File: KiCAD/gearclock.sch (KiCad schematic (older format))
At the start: 39 parts, among them IC1 ATMEGA328P, P10 CD2, P13 CD1, P14 I/O, P15 I/O, P16 I/O, P2 BAT, P4 MOTOR_L, P5 MOTOR_R, P6 LiPo, P7 GPS, P8 FTDI, P9 ISP, SW1 RST, U1 3V3, X1 8MHz

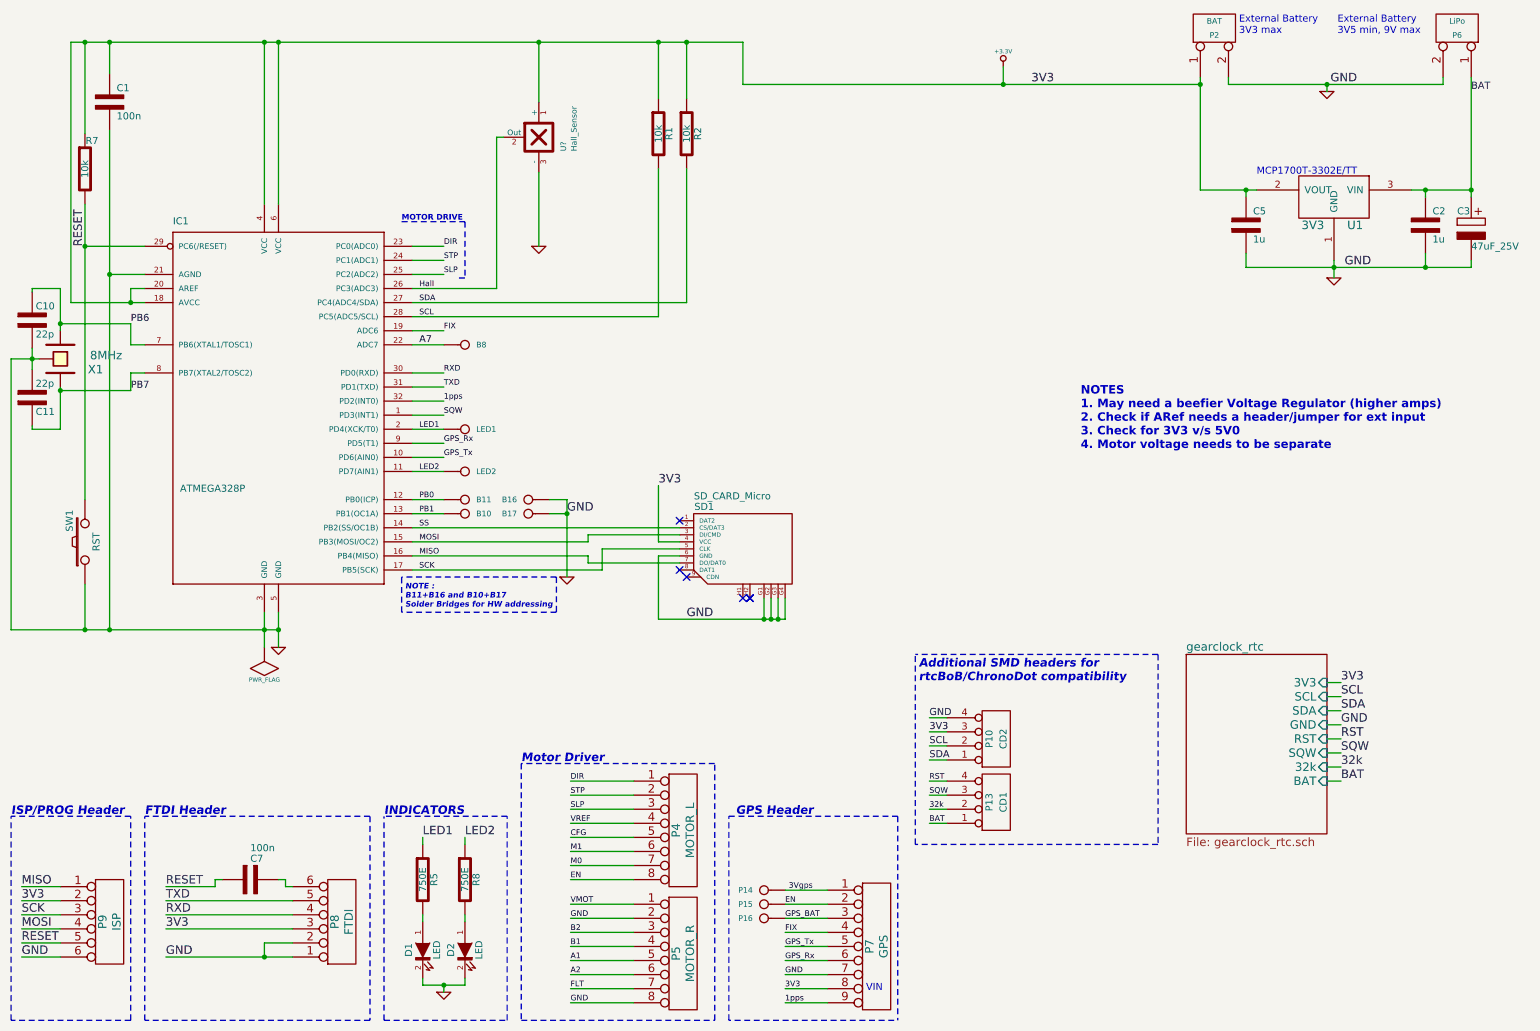
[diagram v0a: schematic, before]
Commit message: GearClock schematic needs review
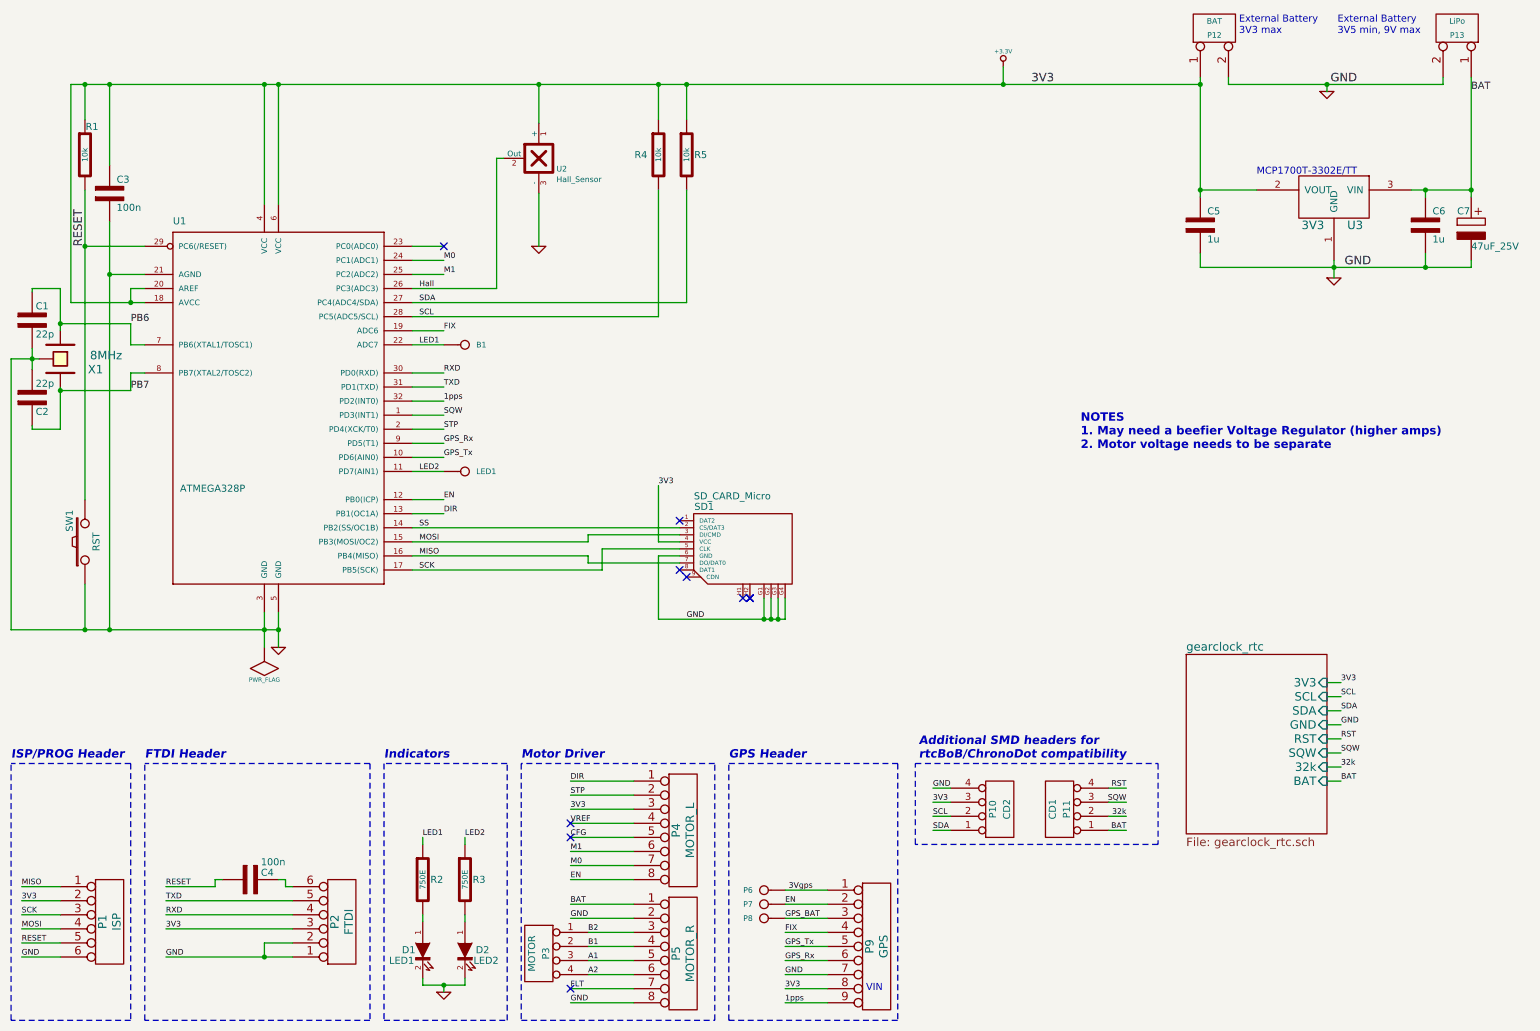
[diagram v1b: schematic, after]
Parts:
- removed B10, B11, B16, B17: I/O, ArthurC Lib:I%2fO_ADR, symbol I/O
- removed LED1: I/O, ArthurC Lib:I%2fO, symbol I/O
- added P3: MOTOR, symbol CONN_4
- D1: value LED -> LED1
- D2: value LED -> LED2
- gave numbers to parts that had none: 1
- renumbered B8 to B1, C10 to C1, C11 to C2, C1 to C3, C7 to C4, C2 to C6, C3 to C7, LED2 to LED1, P9 to P1, P13 to P11, P2 to P12, P6 to P13, P8 to P2, P14 to P6, P15 to P7, P16 to P8, P7 to P9, R7 to R1, R5 to R2, R8 to R3, R1 to R4, R2 to R5, IC1 to U1, U1 to U3
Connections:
- net A7 is gone; now on net LED1: B1.1, U1.22 (ADC7)
- net PB0 is gone; now on net EN: U1.12 (PB0(ICP))
- net PB1 is gone; now on net DIR: U1.13 (PB1(OC1A))
- net VMOT is gone; now on net BAT: P5.1
- net +3.3V: now also P4.3
- net A1: now also P3.3 (P3)
- net A2: now also P3.4 (P4)
- net B1: now also P3.2 (P2)
- net B2: now also P3.1 (P1)
- net DIR: no longer U1.23 (PC0(ADC0))
- net LED1: no longer U1.2 (PD4(XCK/T0))
- net M0: now also U1.24 (PC1(ADC1))
- net M1: now also U1.25 (PC2(ADC2))
- net STP: now also U1.2 (PD4(XCK/T0)); no longer U1.24 (PC1(ADC1))
- removed net SLP: P4.3, U1.25 (PC2(ADC2))
- no-connect marks 6 -> 10
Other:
- note added: "Indicators"
- note added: "NOTES\n1. May need a beefier Voltage Regulator (higher amps)\n2. Motor voltage needs to be separate"
- note removed: "INDICATORS"
- note removed: "MOTOR DRIVE"
- note removed: "NOTE :\nB11+B16 and B10+B17\nSolder Bridges for HW addressing"
- note removed: "NOTES\n1. May need a beefier Voltage Regulator (higher amps)\n2. Check if ARef needs a header/jumper for ext input\n3. Check for 3V3 v/s 5V0\n4. Motor voltage needs to be separate"
- moved on the sheet: C3, C5, P10, P11, R1, R4, R5, U2

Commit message: GearClock schematic mods
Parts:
- P4: value MOTOR_L -> MOTOR_R
- P5: value MOTOR_R -> MOTOR_L
- renumbered B1 to A8, LED1 to D7
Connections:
- net +3.3V: now also P4.6; no longer P4.3
- net CFG: now also P4.4; no longer P4.5
- net DIR: now also P4.8; no longer P4.1
- net EN: now also P4.1; no longer P4.8, P7.1, P9.2
- net Hall: now also U1.22 (ADC7); no longer U1.26 (PC3(ADC3))
- net LED1: now also U1.26 (PC3(ADC3)); no longer U1.22 (ADC7)
- net M0: now also P4.2; no longer P4.7
- net M1: now also P4.3; no longer P4.6
- net STP: now also P4.7; no longer P4.2
- net VREF: now also P4.5; no longer P4.4
- net GPS_EN: now reaches U1.23 (PC0(ADC0))
- net GPS_EN: now also P7.1, P9.2
- no-connect marks 10 -> 9
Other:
- moved on the sheet: A8
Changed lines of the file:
@@
 	3400 2250 3625 2250
 Wire Wire Line
-	3400 2950 3625 2950
+	4000 2950 3400 2950
 Wire Wire Line
 	3400 4150 3625 4150
@@
 	550  4975 2450 4975
 Wire Wire Line
-	4000 1625 4000 2550
-Wire Wire Line
-	4000 2550 3400 2550
+	4000 1625 4000 2950
 Wire Wire Line
 	4300 2250 4300 1875
@@
 P 5325 6400
 F 0 "P4" V 5275 6400 60  0000 C CNN
-F 1 "MOTOR_L" V 5375 6400 60  0000 C CNN
+F 1 "MOTOR_R" V 5375 6400 60  0000 C CNN
 F 2 "ArthurC Lib:PIN_ARRAY-6X1" H 5325 6400 60  0001 C CNN
 F 3 "" H 5325 6400 60  0001 C CNN
 	1    5325 6400
-	1    0    0    -1
+	1    0    0    1
 $EndComp
 Text Label 10000 5650 0    40   ~ 0
@@
 $EndComp
 $Comp
-L I/O B1
+L I/O A8
 U 1 1 4DCD1D4C
-P 3775 2950
-F 0 "B1" H 3855 2950 40  0000 L CNN
-F 1 "I/O" H 3775 3005 30  0001 C CNN
-F 2 "ArthurC Lib:I%2fO" H 3775 2950 60  0001 C CNN
-F 3 "" H 3775 2950 60  0001 C CNN
-	1    3775 2950
+P 3775 2550
+F 0 "A8" H 3855 2550 40  0000 L CNN
+F 1 "I/O" H 3775 2605 30  0001 C CNN
+F 2 "ArthurC Lib:I%2fO" H 3775 2550 60  0001 C CNN
+F 3 "" H 3775 2550 60  0001 C CNN
+	1    3775 2550
 	1    0    0    -1
 $EndComp
@@
 Text Label 3625 2450 0    40   ~ 0
 M1
-Text Label 3450 2550 0    40   ~ 0
+Text Label 3450 2950 0    40   ~ 0
 Hall
 Text Label 3625 3150 0    40   ~ 0
@@
 GPS_BAT
 Text Label 6050 6925 0    40   ~ 0
-EN
+GPS_EN
 Text Label 6050 7125 0    40   ~ 0
 FIX
@@
 Connection ~ 10600 2400
 $Comp
-L I/O LED1
-U 1 1 53809775
-P 3775 3850
-F 0 "LED1" H 3855 3850 40  0000 L CNN
-F 1 "I/O" H 3775 3905 30  0001 C CNN
-F 2 "ArthurC Lib:I%2fO" H 3775 3850 60  0001 C CNN
-F 3 "" H 3775 3850 60  0001 C CNN
-	1    3775 3850
-	1    0    0    -1
-$EndComp
-$Comp
 L CONN_8 P5
 U 1 1 4E241CD6
 P 5325 7275
 F 0 "P5" V 5275 7275 60  0000 C CNN
-F 1 "MOTOR_R" V 5375 7275 60  0000 C CNN
+F 1 "MOTOR_L" V 5375 7275 60  0000 C CNN
 F 2 "ArthurC Lib:PIN_ARRAY-6X1" H 5325 7275 60  0001 C CNN
 F 3 "" H 5325 7275 60  0001 C CNN
@@
 Text Label 4525 6250 0    40   ~ 0
 3V3
-NoConn ~ 3625 2250
 NoConn ~ 4525 7525
-Text Label 3450 2950 0    40   ~ 0
+Text Label 3450 2550 0    40   ~ 0
 LED1
 $Comp
@@
 Wire Notes Line
 	8700 5925 8700 6500
+$Comp
+L I/O D7
+U 1 1 53809775
+P 3775 3850
+F 0 "D7" H 3855 3850 40  0000 L CNN
+F 1 "I/O" H 3775 3905 30  0001 C CNN
+F 2 "ArthurC Lib:I%2fO" H 3775 3850 60  0001 C CNN
+F 3 "" H 3775 3850 60  0001 C CNN
+	1    3775 3850
+	1    0    0    -1
+$EndComp
+Text Label 3625 2250 0    40   ~ 0
+GPS_EN
+Wire Wire Line
+	3400 2550 3625 2550
 $EndSCHEMATC

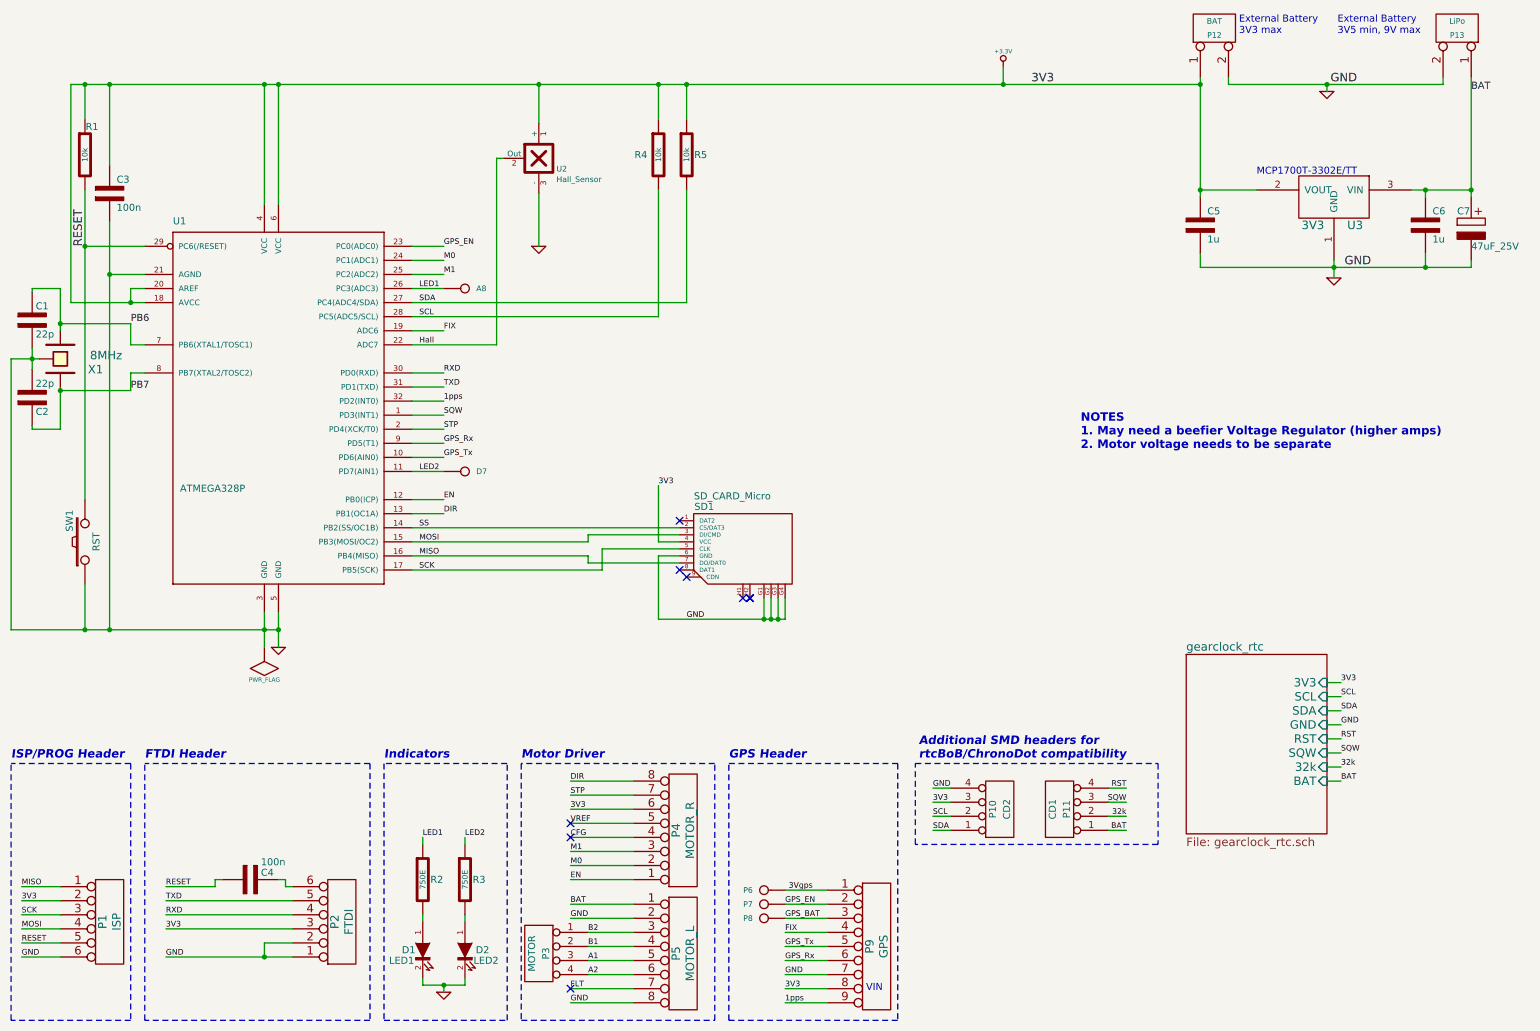
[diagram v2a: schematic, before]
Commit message: GearClock schematic update
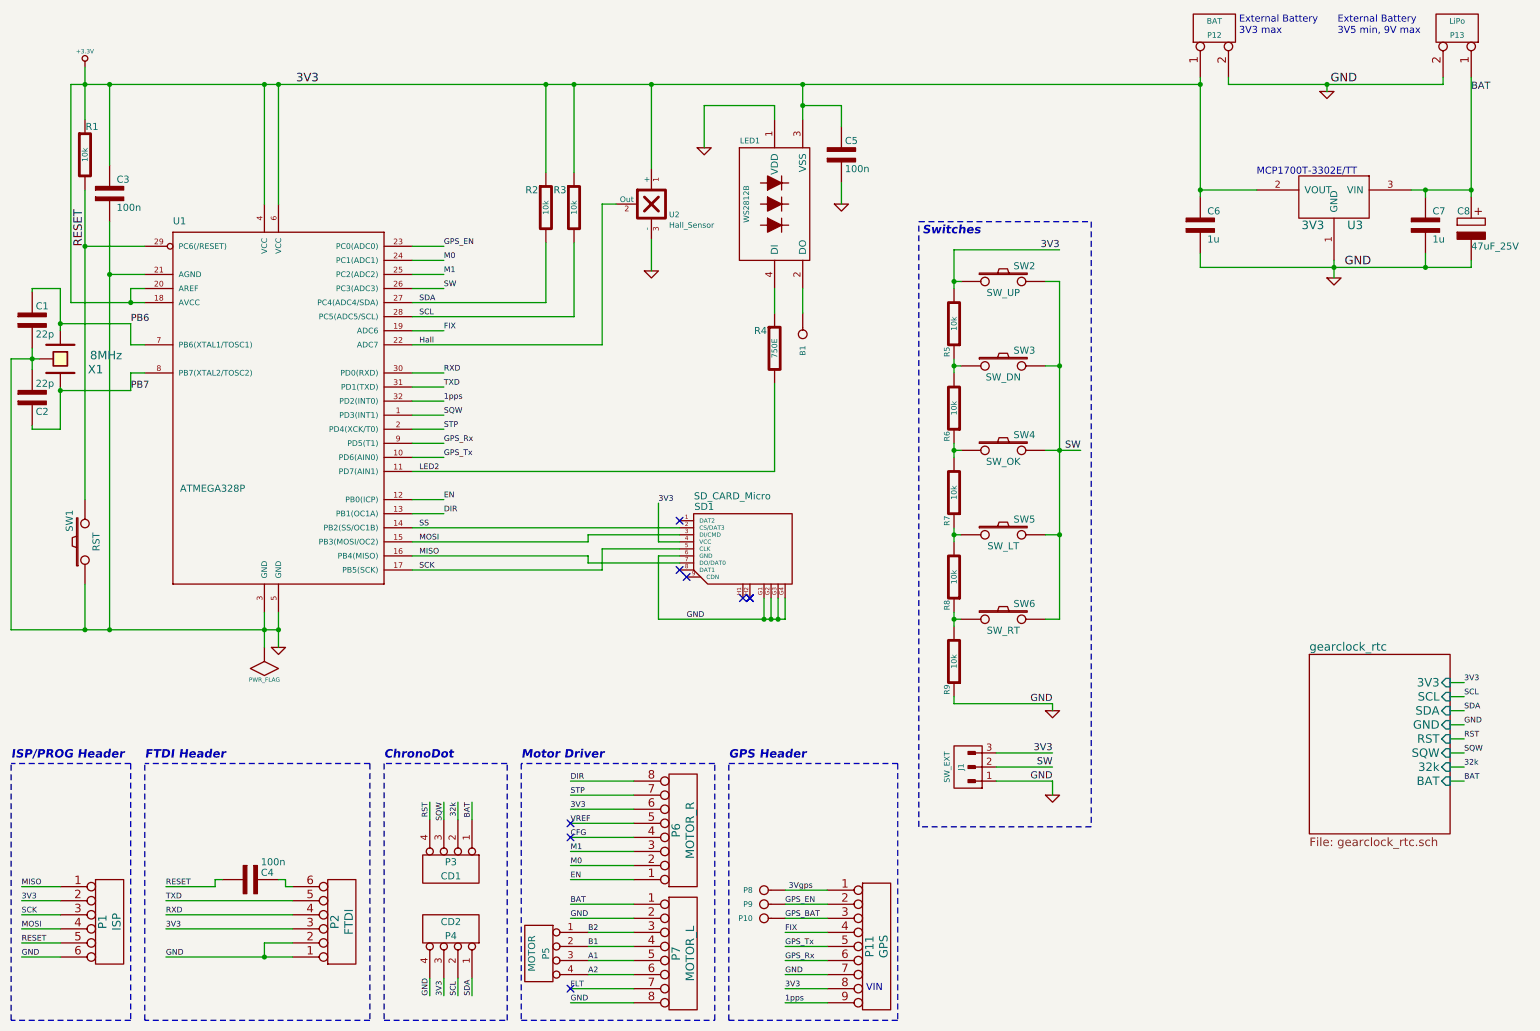
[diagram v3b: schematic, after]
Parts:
- removed A8, D7: I/O, ArthurC Lib:I%2fO, symbol I/O
- removed D1: LED1, ArthurC Lib:d_0805, symbol LED
- removed D2: LED2, ArthurC Lib:d_0805, symbol LED
- removed R3: 750E, ArthurC Lib:r_0805, symbol R
- added B1: I/O, symbol I/O
- added C5: 100n, C4_Pretty:c_0805_led, symbol C
- added J1: SW_EXT, PIN_ARRAY_3x1, symbol CONN_3
- added LED1: WS2812B, C4_Pretty:RGB_WS2811B, symbol WS2812B
- added R5, R6, R7, R8, R9: 10k, r_0805, symbol R
- added SW2: SW_UP, SW-PB, symbol SW_PUSH
- added SW3: SW_DN, SW-PB, symbol SW_PUSH
- added SW4: SW_OK, SW-PB, symbol SW_PUSH
- added SW5: SW_LT, SW-PB, symbol SW_PUSH
- added SW6: SW_RT, SW-PB, symbol SW_PUSH
- renumbered C5 to C6, C6 to C7, C7 to C8, P8 to P10, P9 to P11, P11 to P3, P10 to P4, P3 to P5, P4 to P6, P5 to P7, P6 to P8, P7 to P9, R5 to R2, R4 to R3, R2 to R4
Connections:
- net +3.3V: now also C5.1, J1.3 (P3), LED1.3 (VSS), R5.2, SW2.1
- net GND: now also C5.2, J1.1 (P1), LED1.1 (VDD), R9.1
- net LED2: now also R4.2
- net LED1: no longer names the net of R4.1
- net LED1: now also LED1.4 (DI); no longer U1.26 (PC3(ADC3))
- new net: B1.1, LED1.2 (DO)
- new net: R5.1, R6.2, SW3.1
- new net: R6.1, R7.2, SW4.1
- new net: R7.1, R8.2, SW5.1
- new net: R8.1, R9.2, SW6.1
- new net SW: J1.2 (P2), SW2.2, SW3.2, SW4.2, SW5.2, SW6.2, U1.26 (PC3(ADC3))
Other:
- note added: "ChronoDot"
- note added: "Switches"
- note removed: "Additional SMD headers for\nrtcBoB/ChronoDot compatibility"
- note removed: "Indicators"
- note removed: "NOTES\n1. May need a beefier Voltage Regulator (higher amps)\n2. Motor voltage needs to be separate"
- moved on the sheet: P3, P4, R2, R3, R4, U2
